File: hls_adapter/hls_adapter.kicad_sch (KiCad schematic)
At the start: 5 parts, among them J1 JST B7B-PH-K-S, J2 JST B8B-PH-K-S, J3 Conn_01x04

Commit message: SMW-200 model; HLS adapter
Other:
- title: LDS Breakout -> HLS Adapter
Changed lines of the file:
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@@
   (paper "A5")
   (title_block
-    (title "LDS Breakout")
-    (date "2024-02-02")
+    (title "HLS Adapter")
+    (date "2024-02-13")
     (rev "0.1.0")
     (company "makerspet.com")
@@
     (pin "1")
     (instances
-      (project "lds_breakout"
+      (project "hls_adapter"
         (path "/c13da21a-388e-44a0-831a-aa3d56cf7c53"
           (reference "#PWR02") (unit 1)
@@
     (pin "1")
     (instances
-      (project "lds_breakout"
+      (project "hls_adapter"
         (path "/c13da21a-388e-44a0-831a-aa3d56cf7c53"
           (reference "#PWR05") (unit 1)
@@
     (pin "7")
     (instances
-      (project "lds_breakout"
+      (project "hls_adapter"
         (path "/c13da21a-388e-44a0-831a-aa3d56cf7c53"
           (reference "J1") (unit 1)
@@
     )
     (instances
-      (project "lds_breakout"
+      (project "hls_adapter"
         (path "/c13da21a-388e-44a0-831a-aa3d56cf7c53"
           (reference "H2") (unit 1)
@@
     (pin "1")
     (instances
-      (project "lds_breakout"
+      (project "hls_adapter"
         (path "/c13da21a-388e-44a0-831a-aa3d56cf7c53"
           (reference "#PWR04") (unit 1)
@@
     (pin "1")
     (instances
-      (project "lds_breakout"
+      (project "hls_adapter"
         (path "/c13da21a-388e-44a0-831a-aa3d56cf7c53"
           (reference "J2") (unit 1)
@@
     (pin "3")
     (instances
-      (project "lds_breakout"
+      (project "hls_adapter"
         (path "/c13da21a-388e-44a0-831a-aa3d56cf7c53"
           (reference "J3") (unit 1)
@@
     (pin "1")
     (instances
-      (project "lds_breakout"
+      (project "hls_adapter"
         (path "/c13da21a-388e-44a0-831a-aa3d56cf7c53"
           (reference "#PWR01") (unit 1)
@@
     (pin "1")
     (instances
-      (project "lds_breakout"
+      (project "hls_adapter"
         (path "/c13da21a-388e-44a0-831a-aa3d56cf7c53"
           (reference "#PWR06") (unit 1)
@@
     )
     (instances
-      (project "lds_breakout"
+      (project "hls_adapter"
         (path "/c13da21a-388e-44a0-831a-aa3d56cf7c53"
           (reference "H1") (unit 1)
@@
     (pin "1")
     (instances
-      (project "lds_breakout"
+      (project "hls_adapter"
         (path "/c13da21a-388e-44a0-831a-aa3d56cf7c53"
           (reference "#PWR03") (unit 1)

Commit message: HLS adapter schematic
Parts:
- removed J1: JST B7B-PH-K-S, Connector_JST:JST_PH_B7B-PH-K_1x07_P2.00mm_Vertical, symbol Connector_Generic:Conn_01x07
- removed J3: Conn_01x04, Connector_Molex:Molex_PicoBlade_53398-0471_1x04-1MP_P1.25mm_Vertical, symbol Connector_Generic:Conn_01x04
- added C1: 100uF, Capacitor_SMD:C_1206_3216Metric, symbol Device:C
- added H3, H4: MountingHole, MountingHole:MountingHole_3.2mm_M3, symbol Mechanical:MountingHole
- added J1: JST GH 1.25 6P SKT VERT SMD, Connector_JST:JST_GH_BM06B-GHS-TBT_1x06-1MP_P1.25mm_Vertical, symbol Connector_Generic:Conn_01x06
- added J3: SMW200-H02G 2.0 2P SKT VERT, Makerspet:SMW200_02, symbol Connector_Generic:Conn_01x02
- added J4: JST PH B4B SKT VERT SMD, Connector_JST:JST_PH_B4B-PH-K_1x04_P2.00mm_Vertical, symbol Connector_Generic:Conn_01x04
- J2: value JST B8B-PH-K-S -> Molex PicoBlade 1.25 8P SKT VERT; footprint Connector_JST:JST_PH_B8B-PH-K_1x08_P2.00mm_Vertical -> Connector_Molex:Molex_PicoBlade_53047-0810_1x08_P1.25mm_Vertical
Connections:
- net LDS_MOT_PWM is gone; now on net GND: J2.5 (Pin_5)
- net LDS_TX is gone; now on net +5V: J2.2 (Pin_2)
- net +5V: now also J2.8 (Pin_8), C1.1, J1.6 (Pin_6), J3.2 (Pin_2), J4.1 (Pin_1); no longer J2.1 (Pin_1)
- net GND: now also C1.2, J1.3 (Pin_3), J4.2 (Pin_2); no longer J2.4 (Pin_4)
- net MOT-: now reaches J2.6 (Pin_6)
- net MOT-: now also J2.1 (Pin_1), J1.4 (Pin_4), J3.1 (Pin_1)
- net LDS_EN renamed TX
- net TX: now also J1.5 (Pin_5), J4.4 (Pin_4)
- net LDS_RX: no longer names the net of J2.3 (Pin_3)
- new net RX: J1.2 (Pin_2), J2.4 (Pin_4), J4.3 (Pin_3)
- no-connect marks 3 -> 2
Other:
- note added: "HLS-LFCD02 Logic N/C RX GND PWM TX 5V"
- note added: "HLS-LFCD02 Motor PWM 5V"
- note removed: "YDLIDAR X2/X2L YDLIDAR X3/X3PRO"
- note removed: "YDLIDAR X4"
- title: HLS Adapter -> HLS-LFCD2 Adapter
- moved on the sheet: H1, H2

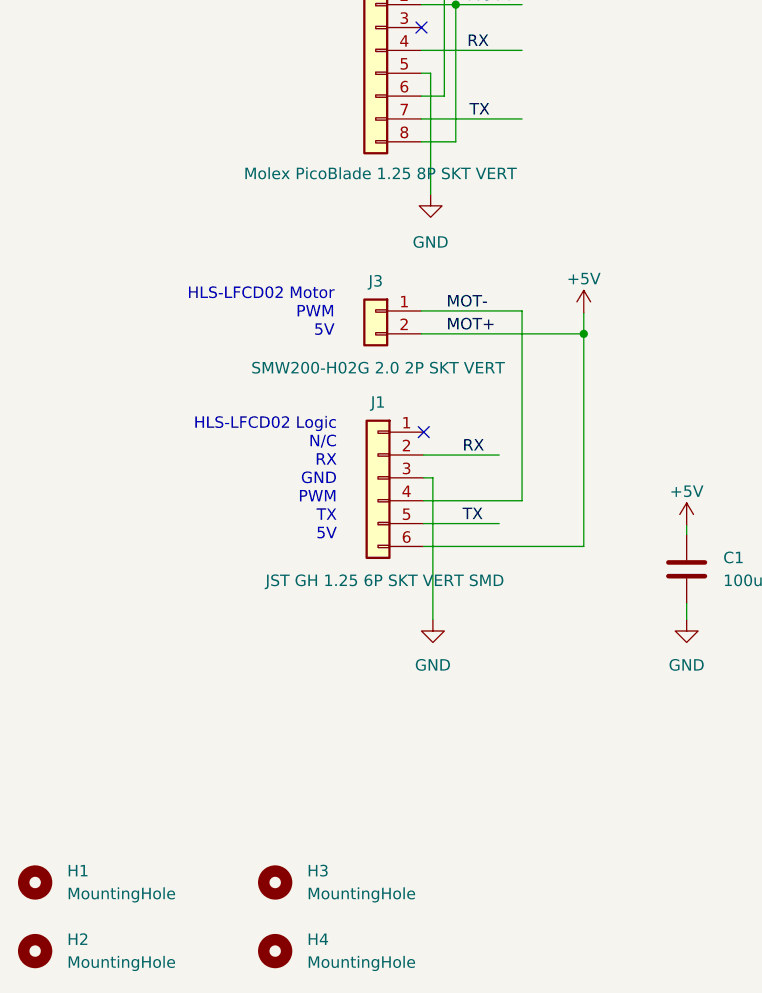
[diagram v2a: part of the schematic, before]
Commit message: HLS Adapter done
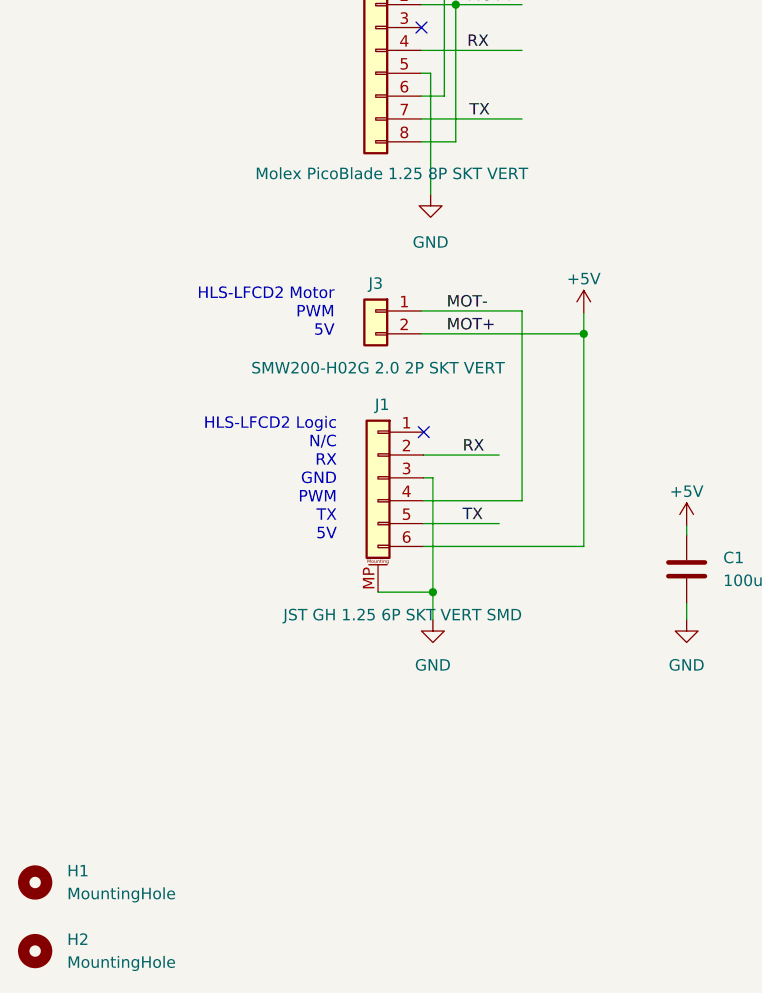
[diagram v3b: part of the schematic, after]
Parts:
- removed H3, H4: MountingHole, MountingHole:MountingHole_3.2mm_M3, symbol Mechanical:MountingHole
- removed J1: JST GH 1.25 6P SKT VERT SMD, Connector_JST:JST_GH_BM06B-GHS-TBT_1x06-1MP_P1.25mm_Vertical, symbol Connector_Generic:Conn_01x06
- added J1: JST GH 1.25 6P SKT VERT SMD, Connector_JST:JST_GH_BM06B-GHS-TBT_1x06-1MP_P1.25mm_Vertical, symbol Connector_Generic_MountingPin:Conn_01x06_MountingPin
- J2: footprint Connector_Molex:Molex_PicoBlade_53047-0810_1x08_P1.25mm_Vertical -> Makerspet:Molex_PicoBlade_53047-0810_1x08_P1.25mm_Vertical
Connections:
- net +5V: now also J1.6 (Pin_6)
- net GND: now also J1.3 (Pin_3), J1.MP (MountPin)
- net MOT-: now also J1.4 (Pin_4)
- net RX: now also J1.2 (Pin_2)
- net TX: now also J1.5 (Pin_5)
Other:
- note added: "HLS-LFCD2 Logic N/C RX GND PWM TX 5V"
- note added: "HLS-LFCD2 Motor PWM 5V"
- note removed: "HLS-LFCD02 Logic N/C RX GND PWM TX 5V"
- note removed: "HLS-LFCD02 Motor PWM 5V"
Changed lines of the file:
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@@
     (company "makerspet.com")
+  )
+  (junction (at 65.532 88.392) (diameter 0) (color 0 0 0 0)
   )
   (junction (at 82.296 59.69) (diameter 0) (color 0 0 0 0)
@@
     (stroke (width 0) (type default))
   )
+  (wire (pts (xy 59.436 88.392) (xy 65.532 88.392))
+    (stroke (width 0) (type default))
+  )
   (wire (pts (xy 64.516 75.692) (xy 65.532 75.692))
     (stroke (width 0) (type default))
@@
     (stroke (width 0) (type default))
   )
+  (wire (pts (xy 65.532 88.392) (xy 65.532 91.44))
+    (stroke (width 0) (type default))
+  )
   (wire (pts (xy 66.802 33.274) (xy 66.802 20.574))
     (stroke (width 0) (type default))
@@
     (stroke (width 0) (type default))
   )
-  (wire (pts (xy 65.532 75.692) (xy 65.532 91.44))
+  (wire (pts (xy 65.532 75.692) (xy 65.532 88.392))
     (stroke (width 0) (type default))
   )
@@
     (stroke (width 0) (type default))
   )
-  (text "HLS-LFCD02 Motor\nPWM\n5V" (at 54.61 60.198 0)
+  (text "HLS-LFCD2 Motor\nPWM\n5V" (at 54.61 60.198 0)
     (effects (font (size 1.27 1.27)) (justify right bottom))
   )
-  (text "HLS-LFCD02 Logic\nN/C\nRX\nGND\nPWM\nTX\n5V" (at 54.864 82.804 0)
+  (text "HLS-LFCD2 Logic\nN/C\nRX\nGND\nPWM\nTX\n5V" (at 54.864 82.804 0)
     (effects (font (size 1.27 1.27)) (justify right bottom))
   )
@@
   (label "MOT-" (at 67.056 57.15 0) (fields_autoplaced)
     (effects (font (size 1.27 1.27)) (justify left bottom))
-  )
-  (symbol (lib_id "Mechanical:MountingHole") (at 48.006 128.27 0) (unit 1)
-    (in_bom no) (on_board yes) (dnp no) (fields_autoplaced)
-    (property "Reference" "H4" (at 51.562 127 0)
-      (effects (font (size 1.27 1.27)) (justify left))
-    )
-    (property "Value" "MountingHole" (at 51.562 129.54 0)
-      (effects (font (size 1.27 1.27)) (justify left))
-    )
-    (property "Footprint" "MountingHole:MountingHole_3.2mm_M3" (at 48.006 128.27 0)
-      (effects (font (size 1.27 1.27)) hide)
-    )
-    (property "Datasheet" "~" (at 48.006 128.27 0)
-      (effects (font (size 1.27 1.27)) hide)
-    )
-    (instances
-      (project "hls_adapter"
-        (path "/c13da21a-388e-44a0-831a-aa3d56cf7c53"
-          (reference "H4") (unit 1)
-        )
-      )
-    )
-  )
-  (symbol (lib_id "Mechanical:MountingHole") (at 48.006 120.65 0) (unit 1)
-    (in_bom no) (on_board yes) (dnp no) (fields_autoplaced)
-    (property "Reference" "H3" (at 51.562 119.38 0)
-      (effects (font (size 1.27 1.27)) (justify left))
-    )
-    (property "Value" "MountingHole" (at 51.562 121.92 0)
-      (effects (font (size 1.27 1.27)) (justify left))
-    )
-    (property "Footprint" "MountingHole:MountingHole_3.2mm_M3" (at 48.006 120.65 0)
-      (effects (font (size 1.27 1.27)) hide)
-    )
-    (property "Datasheet" "~" (at 48.006 120.65 0)
-      (effects (font (size 1.27 1.27)) hide)
-    )
-    (instances
-      (project "hls_adapter"
-        (path "/c13da21a-388e-44a0-831a-aa3d56cf7c53"
-          (reference "H3") (unit 1)
-        )
-      )
-    )
   )
   (symbol (lib_id "power:+5V") (at 93.726 81.026 0) (unit 1)
@@
       (effects (font (size 1.27 1.27)))
     )
-    (property "Value" "Molex PicoBlade 1.25 8P SKT VERT" (at 59.69 41.91 0)
-      (effects (font (size 1.27 1.27)))
-    )
-    (property "Footprint" "Connector_Molex:Molex_PicoBlade_53047-0810_1x08_P1.25mm_Vertical" (at 59.182 28.194 0)
+    (property "Value" "Molex PicoBlade 1.25 8P SKT VERT" (at 60.96 41.91 0)
+      (effects (font (size 1.27 1.27)))
+    )
+    (property "Footprint" "Makerspet:Molex_PicoBlade_53047-0810_1x08_P1.25mm_Vertical" (at 59.182 28.194 0)
       (effects (font (size 1.27 1.27)) hide)
     )
@@
   (symbol (lib_id "Connector_Generic:Conn_01x02") (at 59.182 57.15 0) (mirror y) (unit 1)
     (in_bom yes) (on_board yes) (dnp no)
-    (property "Reference" "J3" (at 59.182 53.848 0)
+    (property "Reference" "J3" (at 59.182 54.102 0)
       (effects (font (size 1.27 1.27)))
     )
@@
     )
   )
-  (symbol (lib_id "Connector_Generic:Conn_01x06") (at 59.436 75.692 0) (mirror y) (unit 1)
+  (symbol (lib_id "Connector_Generic_MountingPin:Conn_01x06_MountingPin") (at 59.436 75.692 0) (mirror y) (unit 1)
     (in_bom yes) (on_board yes) (dnp no)
-    (property "Reference" "J1" (at 59.436 67.31 0)
-      (effects (font (size 1.27 1.27)))
-    )
-    (property "Value" "JST GH 1.25 6P SKT VERT SMD" (at 60.198 87.122 0)
-      (effects (font (size 1.27 1.27)))
+    (property "Reference" "J1" (at 60.706 67.564 0)
+      (effects (font (size 1.27 1.27)) (justify left))
+    )
+    (property "Value" "JST GH 1.25 6P SKT VERT SMD" (at 75.438 90.932 0)
+      (effects (font (size 1.27 1.27)) (justify left))
     )
     (property "Footprint" "Connector_JST:JST_GH_BM06B-GHS-TBT_1x06-1MP_P1.25mm_Vertical" (at 59.436 75.692 0)
@@
     (pin "2")
     (pin "1")
+    (pin "MP")
+    (pin "5")
     (pin "3")
-    (pin "5")
+    (pin "6")
     (pin "4")
-    (pin "6")
-    (instances
-      (project "hls_adapter"
+    (instances
+      (project "hls_adapter"

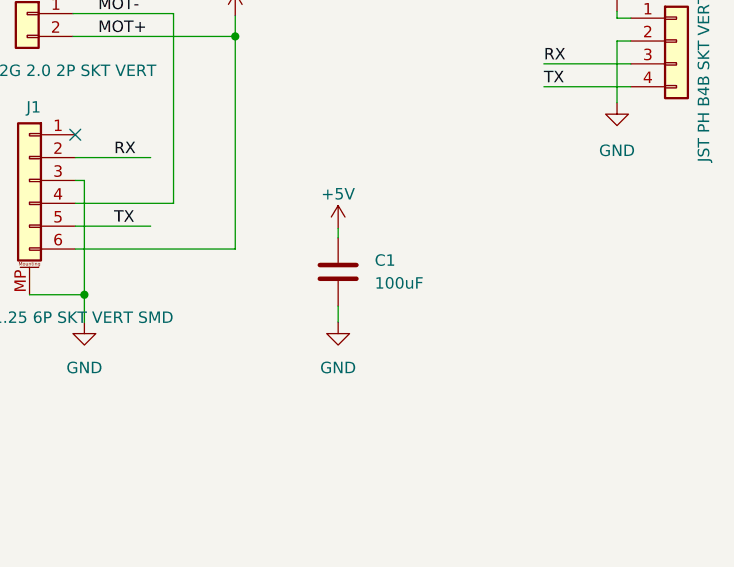
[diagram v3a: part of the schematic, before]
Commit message: ZH extension connector; 6-pin LDS connector
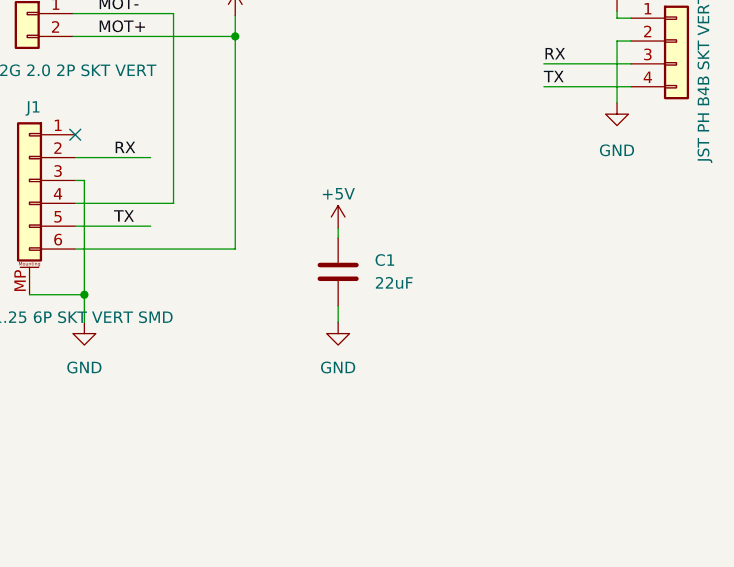
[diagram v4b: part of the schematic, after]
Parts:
- C1: value 100uF -> 22uF; footprint Capacitor_SMD:C_1206_3216Metric -> Capacitor_SMD:C_0603_1608Metric
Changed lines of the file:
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@@
       (effects (font (size 1.27 1.27)) (justify left))
     )
-    (property "Value" "100uF" (at 97.79 87.122 0)
+    (property "Value" "22uF" (at 97.79 87.122 0)
       (effects (font (size 1.27 1.27)) (justify left))
     )
-    (property "Footprint" "Capacitor_SMD:C_1206_3216Metric" (at 94.6912 89.662 0)
+    (property "Footprint" "Capacitor_SMD:C_0603_1608Metric" (at 94.6912 89.662 0)
       (effects (font (size 1.27 1.27)) hide)
     )

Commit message: Schematic notes
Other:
- note added: "HLS-LFCD2 Motor MOT- MOT+ N/C RX GND MOT- TX 5V"
- note added: "Hitachi-LG HLS-LFCD2 Motor PWM 5V"
- note added: "To ESP32 Breakout Board LDS connector 5V GND MOT_EN TX"
- note removed: "HLS-LFCD2 Motor PWM 5V"
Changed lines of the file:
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@@
     (stroke (width 0) (type default))
   )
-  (text "HLS-LFCD2 Motor\nPWM\n5V" (at 54.61 60.198 0)
+  (text "Hitachi-LG\nHLS-LFCD2 Motor\n\nPWM\n5V" (at 54.61 60.198 0)
     (effects (font (size 1.27 1.27)) (justify right bottom))
   )
@@
     (effects (font (size 1.27 1.27)) (justify right bottom))
   )
+  (text "HLS-LFCD2 Motor\n\nMOT-\nMOT+\nN/C\nRX\nGND\nMOT-\nTX\n5V" (at 53.848 36.322 0)
+    (effects (font (size 1.27 1.27)) (justify right bottom))
+  )
+  (text "To ESP32 Breakout\nBoard LDS connector\n\n5V\nGND\nMOT_EN\nTX"
+    (at 137.922 65.024 0)
+    (effects (font (size 1.27 1.27)) (justify left bottom))
+  )
   (label "TX" (at 68.834 80.772 0) (fields_autoplaced)
